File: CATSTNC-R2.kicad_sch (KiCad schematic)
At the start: 48 parts, among them J1 Conn_Coaxial, J1 USB_C_Receptacle_USB2.0, J4 GPIO-1, J5 DC IN, J5 GPIO-2, SW1 RESET, U1 RP2040, U4 NCP1117-3.3_SOT223, U4 NCP1117-5.0_SOT223, U5 W25Q128JVS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

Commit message: Improve design
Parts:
- removed C1: 0.1uF, Capacitor_THT:C_Disc_D3.4mm_W2.1mm_P2.50mm, symbol Device:C
- added C11 (x4): 100nF, Capacitor_SMD:C_0402_1005Metric, symbol Device:C
- added C9: 1uF, Capacitor_SMD:C_0402_1005Metric, symbol Device:C
- C10, C11, C12, C13, C7, C8, C9: footprint Capacitor_SMD:C_0805_2012Metric -> Capacitor_SMD:C_0402_1005Metric
- C3: footprint Capacitor_THT:CP_Radial_D5.0mm_P2.50mm -> Capacitor_SMD:C_0805_2012Metric
- R1, R2, R3, R4, R5, R6: footprint Resistor_SMD:R_0805_2012Metric -> Resistor_SMD:R_0402_1005Metric
- SW1: value RESET -> BOOT
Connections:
- net +1V1: now also C11.1, C11.1
- net +3V3: now also C11.1, C11.1, C9.1
- net D+: now also J1.A6 (D+), J1.B6 (D+); no longer U1.47 (USB_DP)
- net D-: now also J1.A7 (D-), J1.B7 (D-); no longer U1.46 (USB_DM)
- net GND: now also C11.2, C11.2, C11.2, C11.2, C9.2
- net UART_RX: no longer names the net of U1.3 (GPIO1)
- net UART_TX: no longer names the net of U1.2 (GPIO0)
- new net: R3.1, U1.46 (USB_DM)
- new net: R4.1, U1.47 (USB_DP)
- no-connect marks 10 -> 14
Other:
- note added: "UHF Transceiver"
- moved on the sheet: C10, C11, C3, C8, C9, D2, R3, R4, R9, SW1, U1

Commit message: More work
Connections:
- net VBUS renamed VCC
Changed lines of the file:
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@@
+    (stroke (width 0) (type default))
+  )
+  (wire (pts (xy 114.3 41.91) (xy 114.3 43.18))
     (stroke (width 0) (type default))
   )
@@
     )
   )
-  (symbol (lib_id "power:VBUS") (at 114.3 43.18 90) (unit 1)
-    (in_bom yes) (on_board yes) (dnp no)
-    (property "Reference" "#PWR012" (at 118.11 43.18 0)
-      (effects (font (size 1.27 1.27)) hide)
-    )
-    (property "Value" "VBUS" (at 111.76 43.18 90)
-      (effects (font (size 1.27 1.27)) (justify left))
-    )
-    (property "Footprint" "" (at 114.3 43.18 0)
-      (effects (font (size 1.27 1.27)) hide)
-    )
-    (property "Datasheet" "" (at 114.3 43.18 0)
-      (effects (font (size 1.27 1.27)) hide)
-    )
-    (pin "1")
-    (instances
-      (project "PicoBeacon"
-        (path "/333f25f5-6213-47ae-8f1d-b78c72445652"
-          (reference "#PWR012") (unit 1)
-        )
-      )
-      (project "CATSTNC-R2"
-        (path "/4d2f18f9-1900-482a-878f-1242278d07b9"
-          (reference "#PWR033") (unit 1)
-        )
-      )
-    )
-  )
   (symbol (lib_id "power:GND") (at 88.9 39.37 0) (unit 1)
     (in_bom yes) (on_board yes) (dnp no) (fields_autoplaced)
@@
     )
   )
+  (symbol (lib_id "power:VCC") (at 114.3 41.91 0) (unit 1)
+    (in_bom yes) (on_board yes) (dnp no)
+    (property "Reference" "#PWR033" (at 114.3 45.72 0)
+      (effects (font (size 1.27 1.27)) hide)
+    )
+    (property "Value" "VCC" (at 114.3 38.1 0)
+      (effects (font (size 1.27 1.27)))
+    )
+    (property "Footprint" "" (at 114.3 41.91 0)
+      (effects (font (size 1.27 1.27)) hide)
+    )
+    (property "Datasheet" "" (at 114.3 41.91 0)
+      (effects (font (size 1.27 1.27)) hide)
+    )
+    (pin "1")
+    (instances
+      (project "CATSTNC-R2"
+        (path "/4d2f18f9-1900-482a-878f-1242278d07b9"
+          (reference "#PWR033") (unit 1)
+        )
+      )
+    )
+  )
   (symbol (lib_id "power:GND") (at 191.77 102.87 0) (unit 1)
     (in_bom yes) (on_board yes) (dnp no) (fields_autoplaced)
@@
         (path "/4d2f18f9-1900-482a-878f-1242278d07b9"
           (reference "C3") (unit 1)
+        )
+      )
+    )
+  )
+  (symbol (lib_id "power:VCC") (at 34.29 31.75 0) (unit 1)
+    (in_bom yes) (on_board yes) (dnp no)
+    (property "Reference" "#PWR019" (at 34.29 35.56 0)
+      (effects (font (size 1.27 1.27)) hide)
+    )
+    (property "Value" "VCC" (at 34.29 27.94 0)
+      (effects (font (size 1.27 1.27)))
+    )
+    (property "Footprint" "" (at 34.29 31.75 0)
+      (effects (font (size 1.27 1.27)) hide)
+    )
+    (property "Datasheet" "" (at 34.29 31.75 0)
+      (effects (font (size 1.27 1.27)) hide)
+    )
+    (pin "1")
+    (instances
+      (project "CATSTNC-R2"
+        (path "/4d2f18f9-1900-482a-878f-1242278d07b9"
+          (reference "#PWR019") (unit 1)
         )
       )
@@
         )
       )
-    )
-  )
-  (symbol (lib_id "power:VBUS") (at 34.29 31.75 0) (unit 1)
-    (in_bom yes) (on_board yes) (dnp no)
-    (property "Reference" "#PWR019" (at 34.29 35.56 0)
-      (effects (font (size 1.27 1.27)) hide)
-    )
-    (property "Value" "VBUS" (at 34.29 27.94 0)
-      (effects (font (size 1.27 1.27)))
-    )
-    (property "Footprint" "" (at 34.29 31.75 0)
-      (effects (font (size 1.27 1.27)) hide)
-    )
-    (property "Datasheet" "" (at 34.29 31.75 0)
-      (effects (font (size 1.27 1.27)) hide)
-    )
-    (pin "1")
-    (instances
-      (project "CATSTNC-R2"
-        (path "/4d2f18f9-1900-482a-878f-1242278d07b9"
-          (reference "#PWR019") (unit 1)
-        )
-      )

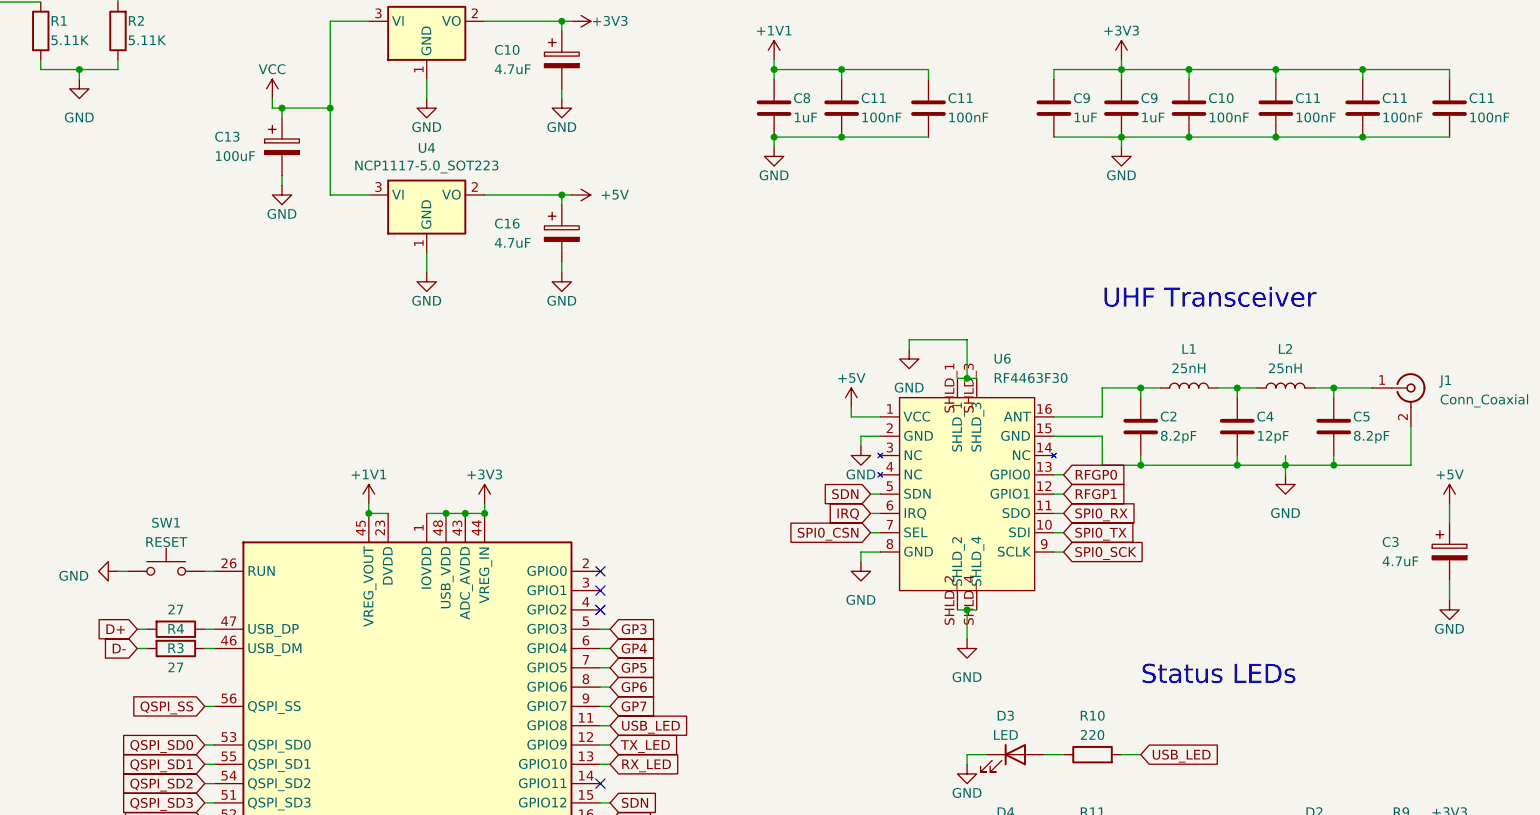
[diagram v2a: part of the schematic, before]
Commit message: Rev 2 Ordered
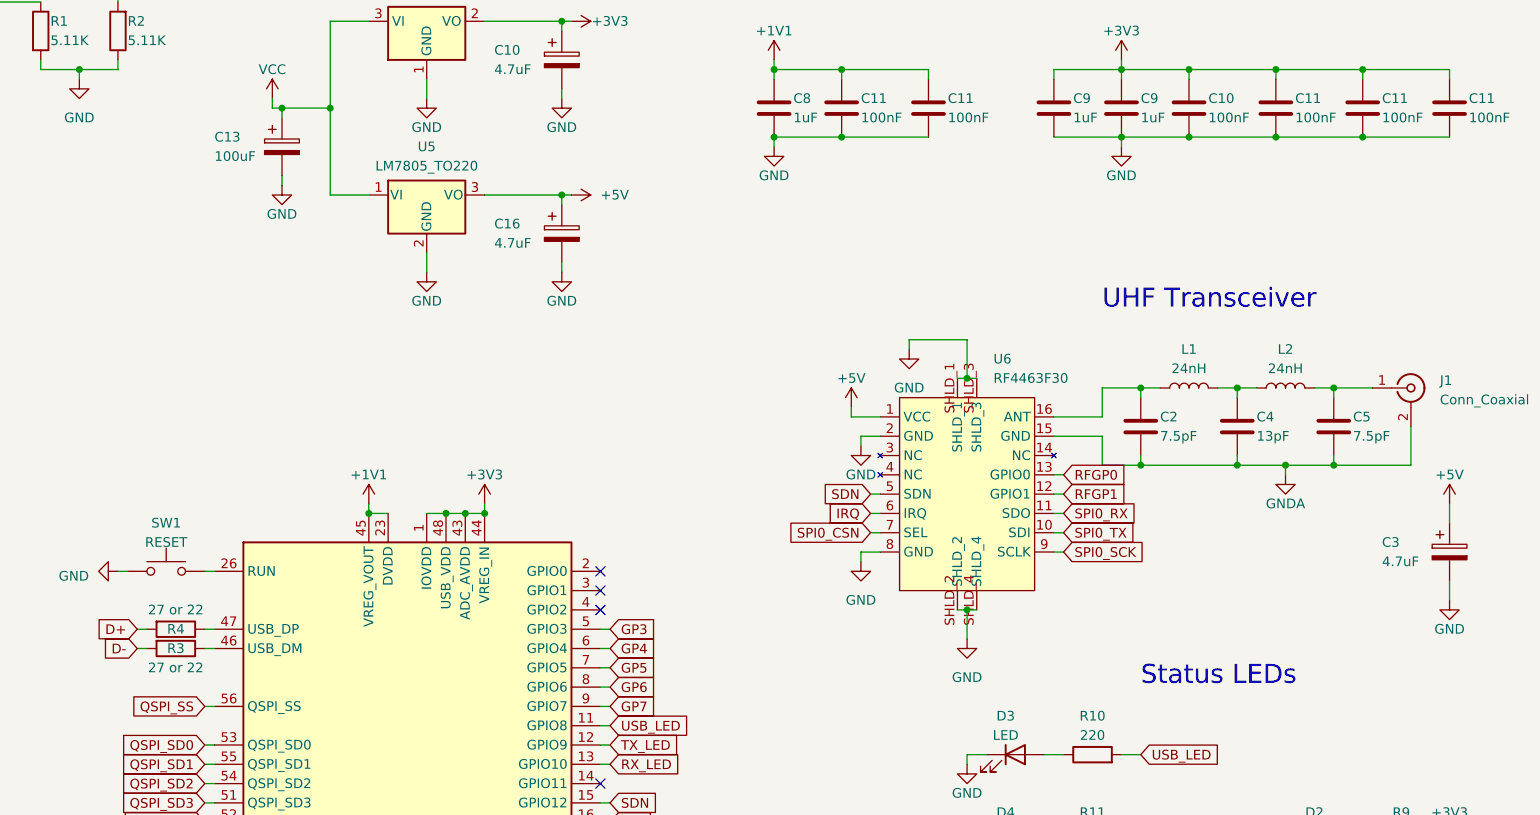
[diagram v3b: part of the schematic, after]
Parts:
- removed U4: NCP1117-5.0_SOT223, Package_TO_SOT_SMD:SOT-223-3_TabPin2, symbol Regulator_Linear:NCP1117-5.0_SOT223
- added U5: LM7805_TO220, Package_TO_SOT_THT:TO-220-3_Vertical, symbol Regulator_Linear:LM7805_TO220
- C2, C5: value 8.2pF -> 7.5pF; footprint Capacitor_THT:C_Disc_D3.4mm_W2.1mm_P2.50mm -> Capacitor_SMD:C_0402_1005Metric
- C4: value 12pF -> 13pF; footprint Capacitor_THT:C_Disc_D3.4mm_W2.1mm_P2.50mm -> Capacitor_SMD:C_0402_1005Metric
- L1, L2: value 25nH -> 24nH; footprint Inductor_THT:L_Toroid_Horizontal_D6.5mm_P10.00mm_Diameter7-5mm_Amidon-T25 -> Inductor_SMD:L_0402_1005Metric
- R3, R4: value 27 -> 27 or 22
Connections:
- net +5V: now also U5.3 (VO)
- net GND: now also U5.2 (GND); no longer C2.2, C4.2, C5.2, J1.2 (Ext), U6.15 (GND)
- net VCC: now also U5.1 (VI)
- new net GNDA: C2.2, C4.2, C5.2, J1.2 (Ext), U6.15 (GND)
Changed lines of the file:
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@@
   (junction (at 189.23 46.99) (diameter 0) (color 0 0 0 0)
   )
+  (junction (at 247.65 90.17) (diameter 0) (color 0 0 0 0)
+  )
   (junction (at 66.04 40.64) (diameter 0) (color 0 0 0 0)
   )
@@
   (junction (at 33.02 44.45) (diameter 0) (color 0 0 0 0)
   )
-  (junction (at 247.65 90.17) (diameter 0) (color 0 0 0 0)
-  )
   (junction (at 254 80.01) (diameter 0) (color 0 0 0 0)
   )
@@
     (stroke (width 0) (type default))
   )
+  (wire (pts (xy 247.65 90.17) (xy 254 90.17))
+    (stroke (width 0) (type default))
+  )
   (wire (pts (xy 246.38 140.97) (xy 248.92 140.97))
     (stroke (width 0) (type default))
@@
     (stroke (width 0) (type default))
   )
+  (wire (pts (xy 247.65 90.17) (xy 247.65 91.44))
+    (stroke (width 0) (type default))
+  )
   (wire (pts (xy 205.74 142.24) (xy 205.74 140.97))
     (stroke (width 0) (type default))
@@
     (stroke (width 0) (type default))
   )
-  (wire (pts (xy 247.65 91.44) (xy 247.65 90.17))
-    (stroke (width 0) (type default))
-  )
   (wire (pts (xy 228.6 153.67) (xy 226.06 153.67))
     (stroke (width 0) (type default))
@@
     (stroke (width 0) (type default))
   )
-  (wire (pts (xy 247.65 90.17) (xy 254 90.17))
-    (stroke (width 0) (type default))
-  )
   (wire (pts (xy 217.17 93.98) (xy 218.44 93.98))
     (stroke (width 0) (type default))
@@
     (stroke (width 0) (type default))
   )
-  (wire (pts (xy 247.65 90.17) (xy 247.65 88.9))
-    (stroke (width 0) (type default))
-  )
   (wire (pts (xy 228.6 90.17) (xy 228.6 88.9))
     (stroke (width 0) (type default))
@@
     )
   )
-  (symbol (lib_id "power:GND") (at 247.65 91.44 0) (unit 1)
-    (in_bom yes) (on_board yes) (dnp no) (fields_autoplaced)
-    (property "Reference" "#PWR017" (at 247.65 97.79 0)
-      (effects (font (size 1.27 1.27)) hide)
-    )
-    (property "Value" "GND" (at 247.65 96.52 0)
-      (effects (font (size 1.27 1.27)))
-    )
-    (property "Footprint" "" (at 247.65 91.44 0)
-      (effects (font (size 1.27 1.27)) hide)
-    )
-    (property "Datasheet" "" (at 247.65 91.44 0)
-      (effects (font (size 1.27 1.27)) hide)
-    )
-    (pin "1")
-    (instances
-      (project "CATSTNC-R2"
-        (path "/4d2f18f9-1900-482a-878f-1242278d07b9"
-          (reference "#PWR017") (unit 1)
-        )
-      )
-    )
-  )
   (symbol (lib_id "power:GND") (at 54.61 152.4 0) (unit 1)
     (in_bom yes) (on_board yes) (dnp no) (fields_autoplaced)
@@
       (effects (font (size 1.27 1.27)))
     )
-    (property "Value" "25nH" (at 247.65 77.47 90)
+    (property "Value" "24nH" (at 247.65 77.47 90)
       (effects (font (size 1.27 1.27)))
     )
-    (property "Footprint" "Inductor_THT:L_Toroid_Horizontal_D6.5mm_P10.00mm_Diameter7-5mm_Amidon-T25" (at 247.65 80.01 0)
+    (property "Footprint" "Inductor_SMD:L_0402_1005Metric" (at 247.65 80.01 0)
       (effects (font (size 1.27 1.27)) hide)
     )
@@
       (effects (font (size 1.27 1.27)) (justify left))
     )
-    (property "Value" "8.2pF" (at 231.14 86.36 0)
+    (property "Value" "7.5pF" (at 231.14 86.36 0)
       (effects (font (size 1.27 1.27)) (justify left))
     )
-    (property "Footprint" "Capacitor_THT:C_Disc_D3.4mm_W2.1mm_P2.50mm" (at 229.5652 88.9 0)
+    (property "Footprint" "Capacitor_SMD:C_0402_1005Metric" (at 229.5652 88.9 0)
       (effects (font (size 1.27 1.27)) hide)
     )
@@
       (effects (font (size 1.27 1.27)) (justify left))
     )
-    (property "Value" "8.2pF" (at 256.54 86.36 0)
+    (property "Value" "7.5pF" (at 256.54 86.36 0)
       (effects (font (size 1.27 1.27)) (justify left))
     )
-    (property "Footprint" "Capacitor_THT:C_Disc_D3.4mm_W2.1mm_P2.50mm" (at 254.9652 88.9 0)
+    (property "Footprint" "Capacitor_SMD:C_0402_1005Metric" (at 254.9652 88.9 0)
       (effects (font (size 1.27 1.27)) hide)
     )
@@
       (effects (font (size 1.27 1.27)) (justify left))
     )
-    (property "Value" "12pF" (at 243.84 86.36 0)
+    (property "Value" "13pF" (at 243.84 86.36 0)
       (effects (font (size 1.27 1.27)) (justify left))
     )
-    (property "Footprint" "Capacitor_THT:C_Disc_D3.4mm_W2.1mm_P2.50mm" (at 242.2652 88.9 0)
+    (property "Footprint" "Capacitor_SMD:C_0402_1005Metric" (at 242.2652 88.9 0)
       (effects (font (size 1.27 1.27)) hide)
     )
@@
     )
   )
+  (symbol (lib_id "Regulator_Linear:LM7805_TO220") (at 134.62 54.61 0) (unit 1)
+    (in_bom yes) (on_board yes) (dnp no) (fields_autoplaced)
+    (property "Reference" "U5" (at 134.62 48.26 0)
+      (effects (font (size 1.27 1.27)))
+    )
+    (property "Value" "LM7805_TO220" (at 134.62 50.8 0)
+      (effects (font (size 1.27 1.27)))
+    )
+    (property "Footprint" "Package_TO_SOT_THT:TO-220-3_Vertical" (at 134.62 48.895 0)
+      (effects (font (size 1.27 1.27) italic) hide)
+    )
+    (property "Datasheet" "https://www.onsemi.cn/PowerSolutions/document/MC7800-D.PDF" (at 134.62 55.88 0)
+      (effects (font (size 1.27 1.27)) hide)
+    )
+    (pin "1")
+    (pin "3")
+    (pin "2")
+    (instances
+      (project "CATSTNC-R2"
+        (path "/4d2f18f9-1900-482a-878f-1242278d07b9"
+          (reference "U5") (unit 1)
+        )
+      )
+    )
+  )
   (symbol (lib_id "Device:L") (at 234.95 80.01 90) (unit 1)
     (in_bom yes) (on_board yes) (dnp no) (fields_autoplaced)
@@
       (effects (font (size 1.27 1.27)))
     )
-    (property "Value" "25nH" (at 234.95 77.47 90)
+    (property "Value" "24nH" (at 234.95 77.47 90)
       (effects (font (size 1.27 1.27)))
     )
-    (property "Footprint" "Inductor_THT:L_Toroid_Horizontal_D6.5mm_P10.00mm_Diameter7-5mm_Amidon-T25" (at 234.95 80.01 0)
+    (property "Footprint" "Inductor_SMD:L_0402_1005Metric" (at 234.95 80.01 0)
       (effects (font (size 1.27 1.27)) hide)
     )
@@
       (effects (font (size 1.27 1.27)))
     )
-    (property "Value" "27" (at 101.6 109.22 90)
+    (property "Value" "27 or 22" (at 101.6 109.22 90)
       (effects (font (size 1.27 1.27)))
     )
@@
     )
   )
+  (symbol (lib_id "power:GNDA") (at 247.65 91.44 0) (unit 1)
+    (in_bom yes) (on_board yes) (dnp no)
+    (property "Reference" "#PWR017" (at 247.65 97.79 0)
+      (effects (font (size 1.27 1.27)) hide)
+    )
+    (property "Value" "GNDA" (at 247.65 95.25 0)
+      (effects (font (size 1.27 1.27)))
+    )
+    (property "Footprint" "" (at 247.65 91.44 0)
+      (effects (font (size 1.27 1.27)) hide)
+    )
+    (property "Datasheet" "" (at 247.65 91.44 0)
+      (effects (font (size 1.27 1.27)) hide)
+    )
+    (pin "1")
+    (instances
+      (project "CATSTNC-R2"
+        (path "/4d2f18f9-1900-482a-878f-1242278d07b9"
+          (reference "#PWR017") (unit 1)
+        )
+      )
+    )
+  )
   (symbol (lib_id "Connector:Barrel_Jack_MountingPin") (at 25.4 35.56 0) (unit 1)
     (in_bom yes) (on_board yes) (dnp no)
@@
       (effects (font (size 1.27 1.27)))
     )
-    (property "Value" "27" (at 101.6 116.84 90)
+    (property "Value" "27 or 22" (at 101.6 116.84 90)
       (effects (font (size 1.27 1.27)))
     )
@@
         )
       )
-    )
-  )
-  (symbol (lib_id "Regulator_Linear:NCP1117-5.0_SOT223") (at 134.62 54.61 0) (unit 1)
-    (in_bom yes) (on_board yes) (dnp no)
-    (property "Reference" "U4" (at 134.62 48.4632 0)
-      (effects (font (size 1.27 1.27)))
-    )
-    (property "Value" "NCP1117-5.0_SOT223" (at 134.62 50.7746 0)
-      (effects (font (size 1.27 1.27)))
-    )
-    (property "Footprint" "Package_TO_SOT_SMD:SOT-223-3_TabPin2" (at 134.62 49.53 0)
-      (effects (font (size 1.27 1.27)) hide)
-    )
-    (property "Datasheet" "http://www.onsemi.com/pub_link/Collateral/NCP1117-D.PDF" (at 137.16 60.96 0)
-      (effects (font (size 1.27 1.27)) hide)
-    )
-    (pin "1")
-    (pin "2")
-    (pin "3")
-    (instances
-      (project "PicoBeacon"
-        (path "/333f25f5-6213-47ae-8f1d-b78c72445652"
-          (reference "U4") (unit 1)
-        )
-      )
-      (project "RP2040_minimal"
-        (path "/46b710fe-28e0-4aef-b489-e47c9d99ae26"
-          (reference "U1") (unit 1)
-        )
-      )
-      (project "CATSTNC-R2"
-        (path "/4d2f18f9-1900-482a-878f-1242278d07b9"
-          (reference "U1") (unit 1)
-        )
-      )

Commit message: Start work on Rev 3
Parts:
- removed C13: 100uF, Capacitor_THT:CP_Radial_D5.0mm_P2.50mm, symbol Device:C_Polarized
- removed U5: LM7805_TO220, Package_TO_SOT_THT:TO-220-3_Vertical, symbol Regulator_Linear:LM7805_TO220
- added C1, C23, C24: 100nF, Capacitor_SMD:C_0603_1608Metric, symbol Device:C
- added C21, C22: 22uF, Capacitor_SMD:C_0603_1608Metric, symbol Device:C
- added C25, C26: 10uF, Capacitor_SMD:C_0805_2012Metric, symbol Device:C
- added C27: 33nF, Capacitor_SMD:C_0603_1608Metric, symbol Device:C
- added D1: BAT54C, Package_TO_SOT_SMD:SOT-23, symbol Diode:BAT54C
- added L3: 6.8uH, Inductor_SMD:L_Sunlord_SWPA6020S, symbol Device:L
- added R1: 54.9K 1%, Resistor_SMD:R_0402_1005Metric, symbol Device:R
- added R13: 0, Resistor_SMD:R_0603_1608Metric, symbol Device:R
- added R2: 10.0K 1%, Resistor_SMD:R_0402_1005Metric, symbol Device:R
- added U1: TPS62933, Package_TO_SOT_SMD:SOT-583-8, symbol Regulator_Switching:TPS62933
- C10, C16: footprint Capacitor_THT:CP_Radial_D5.0mm_P2.50mm -> Capacitor_SMD:C_1206_3216Metric
- J1: value Conn_Coaxial -> BNC
- R1, R2: symbol Device:R -> Device:R_Small
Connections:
- net +5V: now also U4.3 (VI), D1.3; no longer C16.1
- net GND: now also C21.2, C22.2, C23.2, C24.2, C25.2, C26.2, C27.2, R13.2, R2.2, U1.4 (GND)
- net VCC: now also C16.1, C24.1, C25.1, C26.1, U1.3 (VIN); no longer U4.3 (VI)
- net USB_VBUS: now reaches J1.A4 (VBUS), J1.A9 (VBUS), J1.B4 (VBUS), J1.B9 (VBUS)
- net USB_VBUS: now also D1.1
- net XIN: no longer names the net of C12.1, U1.20 (XIN), Y2.3
- net XOUT: no longer names the net of R6.1, U1.21 (XOUT)
- new net: C27.1, U1.7 (SS)
- new net: C1.2, L3.1, U1.5 (SW)
- new net: C1.1, U1.6 (BST)
- new net REG_5V: C21.1, C22.1, C23.1, D1.2, L3.2, R1.1
- new net RT: R13.1, U1.1 (RT)
- new net VFB: R1.2, R2.1, U1.8 (FB)
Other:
- note added: "Microcontroller"
- note added: "Mounting Holes"
- note added: "Power"
- note added: "USB"
- note removed: "Power Supply"
- moved on the sheet: C10, C11, C12, C13, C16, C2, C3, C4, C5, C7, C8, C9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
